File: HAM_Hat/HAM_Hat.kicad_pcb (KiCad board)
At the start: 2 copper layers, 65 x 56.5 mm, 48 parts, among them J101 TL212V-02P-G12S, J102 DB-9RS-C, J103 NCW254-02S, J104 SMA6252A2, J109 socket, J3 FHDH2.54-40, M101 Fan, Q101 BSS138, Q102 BSS138, Q103 BSS138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

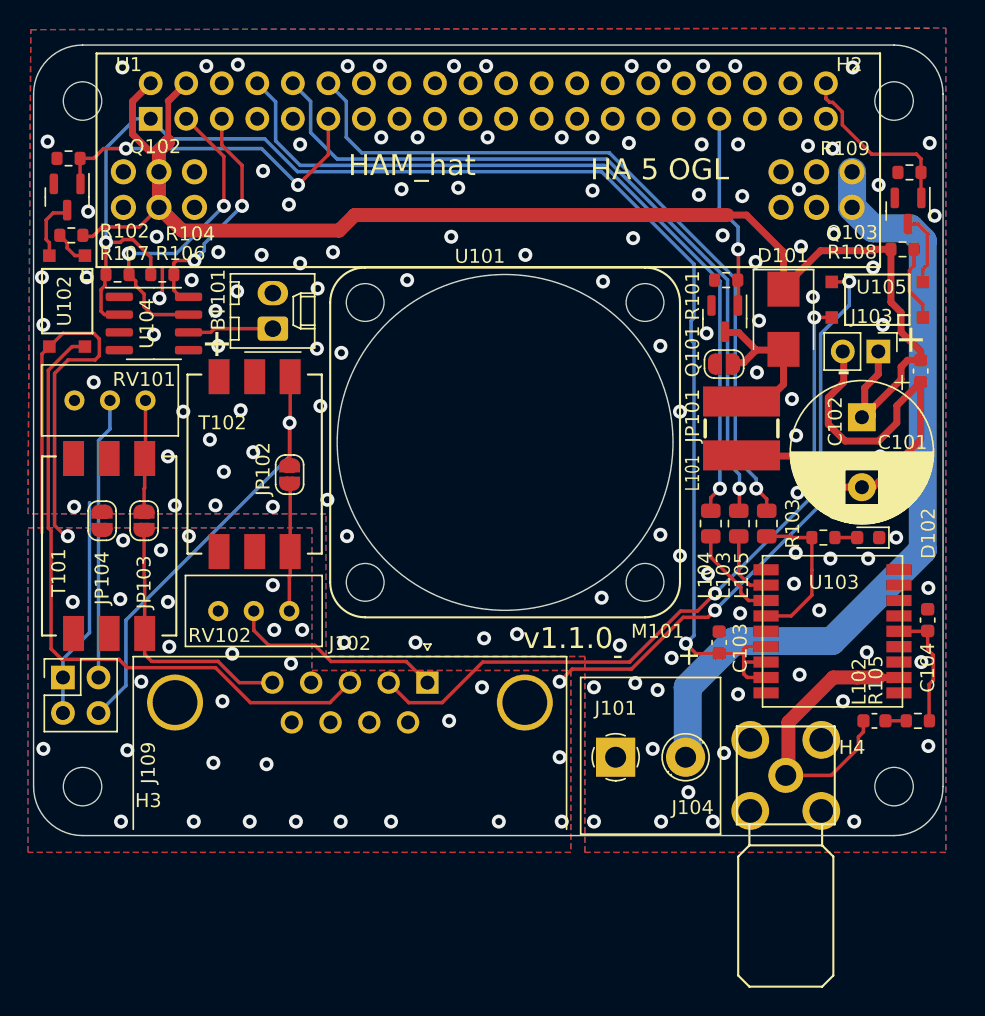
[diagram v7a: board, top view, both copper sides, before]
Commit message: Add 0.5mm edge clearence to copper.
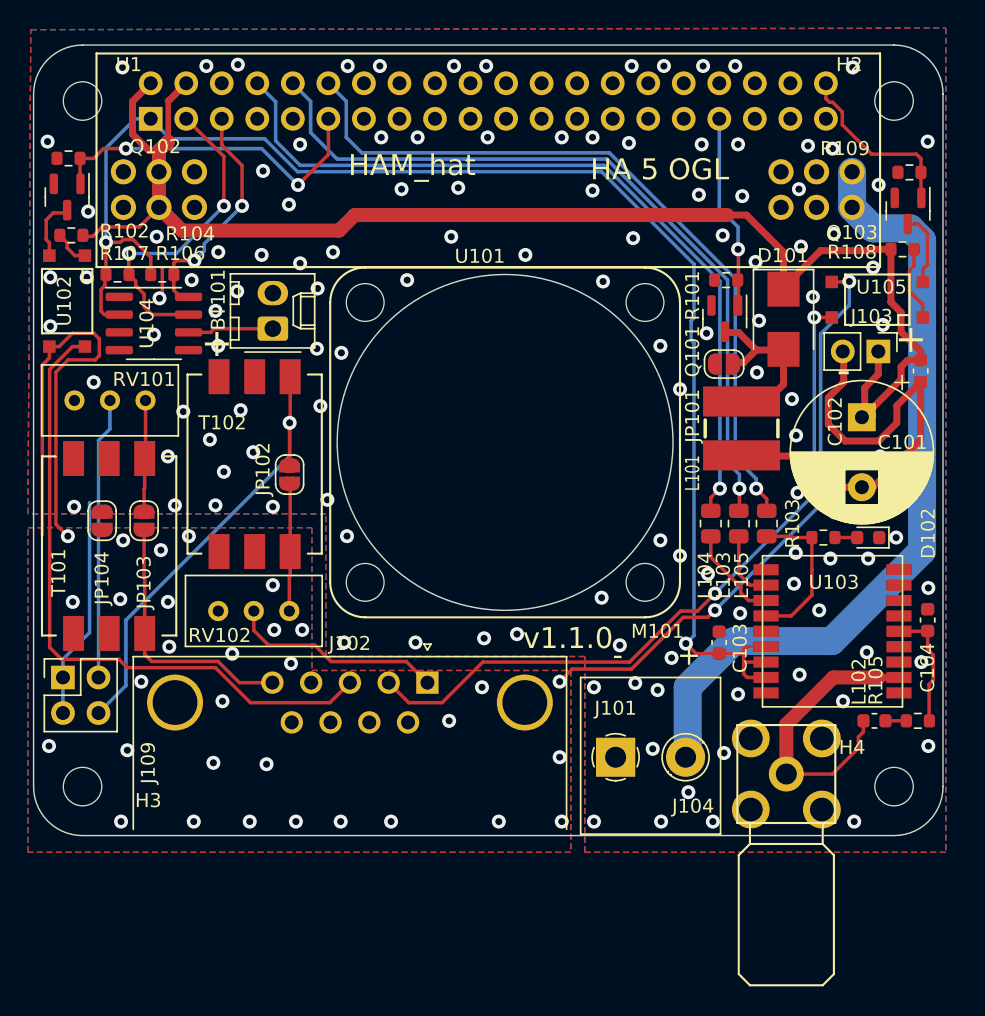
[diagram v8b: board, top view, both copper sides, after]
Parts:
- moved J104 0.11 mm to (169.8, 121.6)
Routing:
- net GND: vias 125 -> 124
